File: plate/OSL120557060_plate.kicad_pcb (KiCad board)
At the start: 2 copper layers, 115.6 x 108 mm, 2 parts

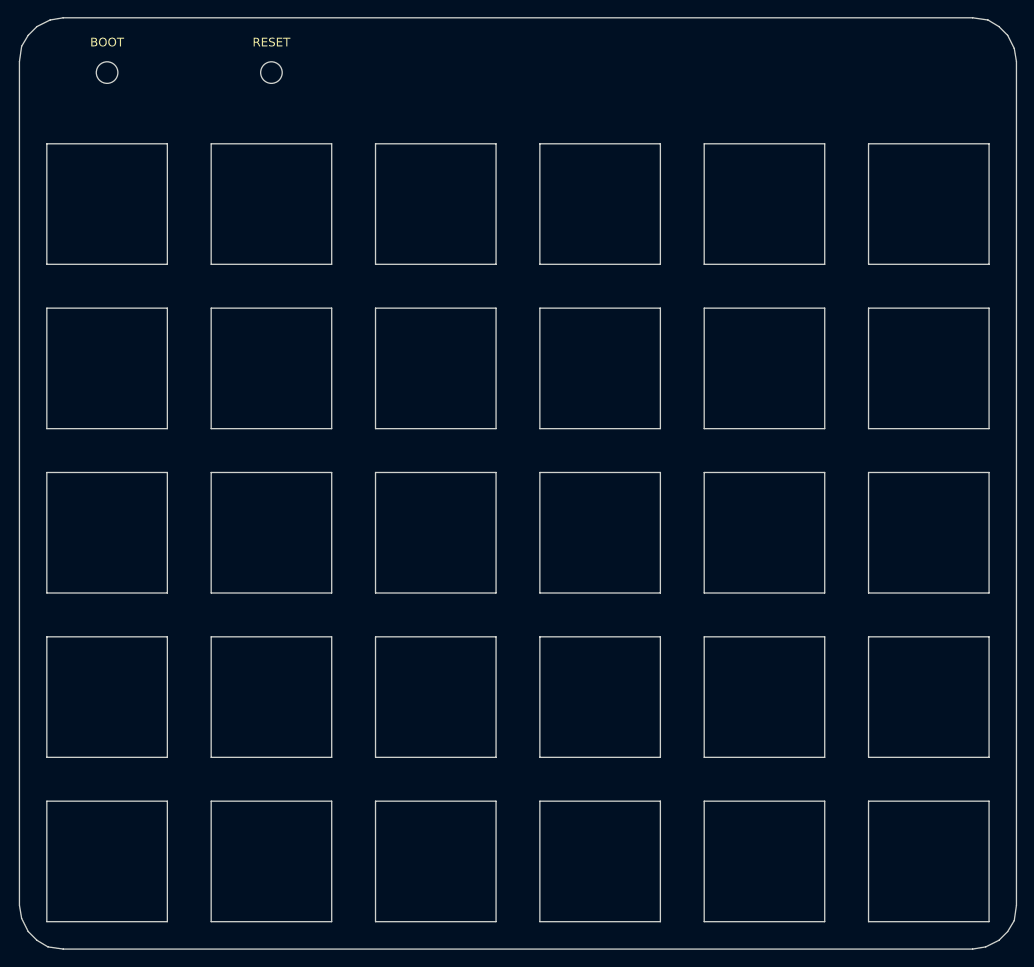
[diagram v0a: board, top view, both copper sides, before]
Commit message: * added mount pis to pcb * improved plate layout
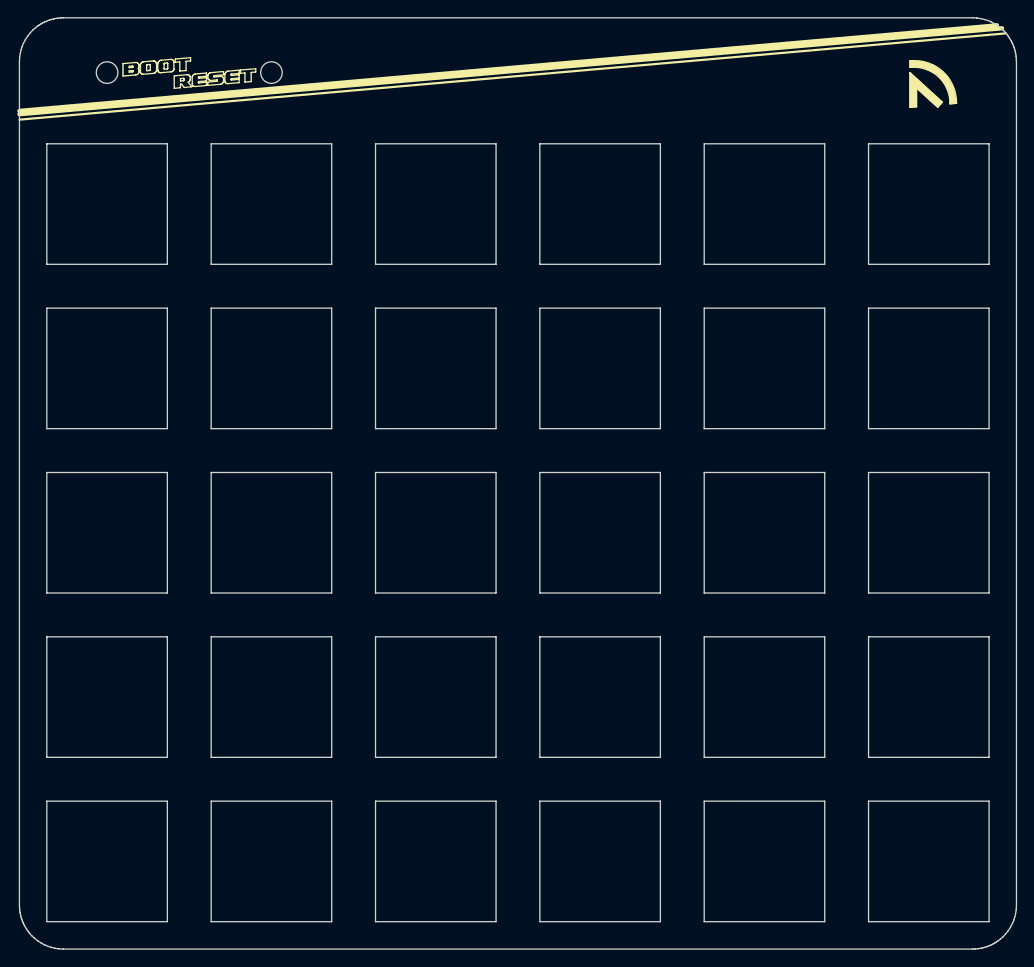
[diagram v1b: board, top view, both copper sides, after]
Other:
- outline, holes or cut-outs redrawn
